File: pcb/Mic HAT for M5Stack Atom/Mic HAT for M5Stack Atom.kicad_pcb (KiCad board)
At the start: 2 copper layers, 21 x 37.8 mm, 17 parts, among them J1 Atom Left, J2 Atom Right, J3 INMP441 Left, J4 INMP441 Right

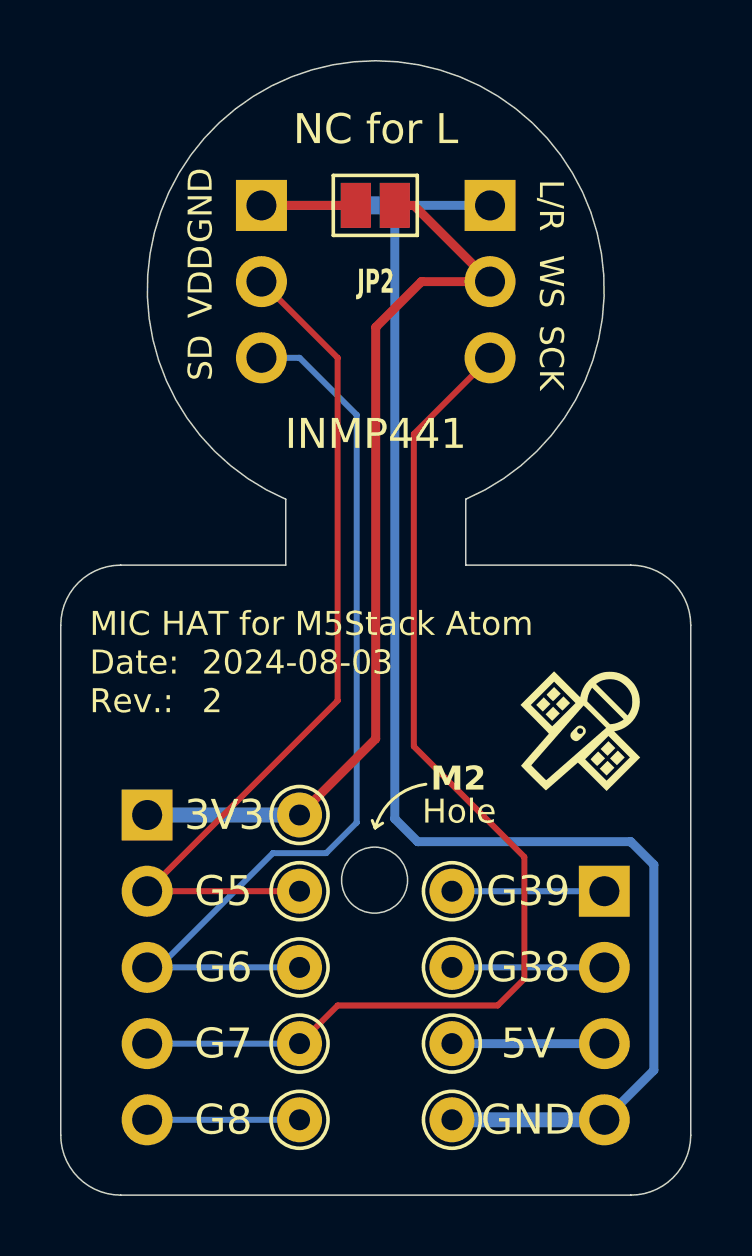
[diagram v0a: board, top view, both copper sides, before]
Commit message: rev. 3, fixed big oopsy reversed headers, aligned hole and some silkscreen alignments
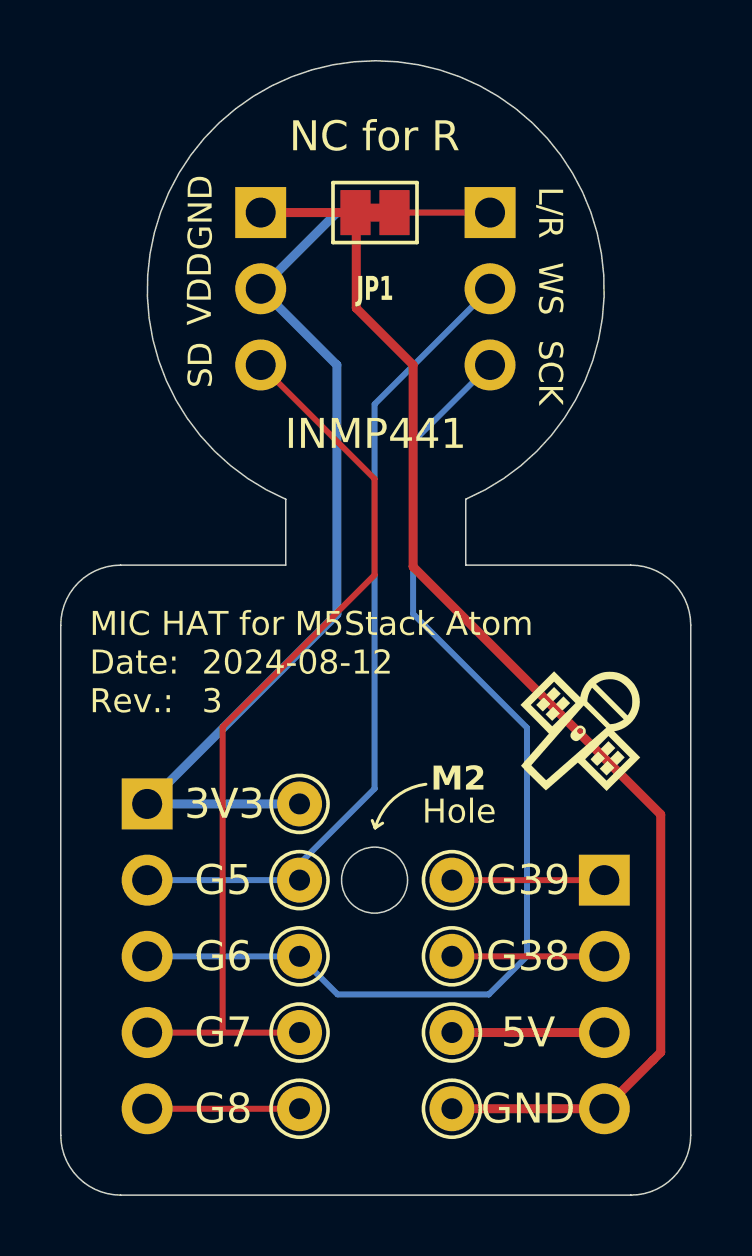
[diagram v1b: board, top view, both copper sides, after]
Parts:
- JP1: moved to F.Cu
- JP2: moved to B.Cu
- moved J4 7.65 mm to (119.4, 53.6)
- moved J3 7.62 mm to (127.0, 53.6)
- moved 3V3 0.37 mm to (120.7, 73.3)
- moved 5V1 0.37 mm to (125.7, 80.9)
- moved G38 0.37 mm to (125.7, 78.4)
- moved G39 0.37 mm to (125.7, 75.8)
- moved G5 0.37 mm to (120.7, 75.8)
- moved G6 0.37 mm to (120.7, 78.4)
- moved G7 0.37 mm to (120.7, 80.9)
- moved G8 0.37 mm to (120.7, 83.5)
- moved GND1 0.37 mm to (125.7, 83.5)
- moved J1 0.37 mm to (115.6, 73.3)
- moved J2 0.37 mm to (130.8, 75.8)
- moved JP1 0.24 mm to (123.2, 53.6), turned to 180 degrees
- moved JP2 0.24 mm to (123.2, 53.6), turned to 0 degrees
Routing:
- net /SD: track 36.7 -> 31.0 mm
- net /SCK: track 31.6 -> 36.1 mm
- net GND: track 47.2 -> 43.1 mm
- net /WS: track 29.1 -> 27.4 mm
- net +3V3: track 31.1 -> 30.1 mm
